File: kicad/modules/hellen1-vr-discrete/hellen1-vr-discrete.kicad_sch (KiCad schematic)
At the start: 45 parts, among them M1 Module-vr-discrete-0.1, U1 74AHC1G02, U2 74AHC1G02, U751 SRV05-4, U753 MCP6004, U754 MAX9142, U755 NC7SB3157P6X, U756 NC7SB3157P6X

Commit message: vr-discrete: rename SRV05-4-P-T7 in kicad
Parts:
- U751: value SRV05-4 -> SRV05-4-P-T7
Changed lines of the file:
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@@
     (in_bom yes) (on_board yes)
     (property "Reference" "U751" (id 0) (at 76.2 30.48 0))
-    (property "Value" "SRV05-4" (id 1) (at 72.39 26.67 0)
+    (property "Value" "SRV05-4-P-T7" (id 1) (at 72.39 26.67 0)
       (effects (font (size 1.27 1.27)) hide)
     )
@@
     )
     (path "/2438cbe3-a2c4-4bca-9f38-14e827595b8e"
-      (reference "U751") (unit 1) (value "SRV05-4") (footprint "Package_TO_SOT_SMD:SOT-23-6")
+      (reference "U751") (unit 1) (value "SRV05-4-P-T7") (footprint "Package_TO_SOT_SMD:SOT-23-6")
     )
     (path "/4fab11ed-4e08-402e-943d-dbc4e18c69da"

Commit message: fix BOM/LED-GREEN-0603 for vr-discrete
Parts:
- D751: value LED -> LED-GREEN-0603
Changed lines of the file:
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@@
       (effects (font (size 1.27 1.27)) (justify right))
     )
-    (property "Value" "LED" (id 1) (at 33.4772 128.3208 90)
+    (property "Value" "LED-GREEN-0603" (id 1) (at 33.4772 128.3208 90)
       (effects (font (size 1.27 1.27)) (justify right))
     )
@@
     )
     (path "/f48b53a5-a1a7-45f8-861f-0a454ab7dbf2"
-      (reference "D751") (unit 1) (value "LED") (footprint "LED_SMD:LED_0603_1608Metric")
+      (reference "D751") (unit 1) (value "LED-GREEN-0603") (footprint "LED_SMD:LED_0603_1608Metric")
     )
     (path "/c56f9b22-fce5-4a58-bfa9-904429ba6336"

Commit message: vr-discrete: fix designator numbering
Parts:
- renumbered C1 to C761, M1 to M750, U1 to U752, U2 to U757
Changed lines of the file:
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@@
   (symbol (lib_id "Device:C") (at 219.71 77.47 0) (unit 1)
     (in_bom yes) (on_board yes)
-    (property "Reference" "C1" (id 0) (at 222.631 76.3016 0)
+    (property "Reference" "C761" (id 0) (at 222.631 76.3016 0)
       (effects (font (size 1.27 1.27)) (justify left))
     )
@@
   (symbol (lib_id "74xGxx:74AHC1G02") (at 203.2 64.77 0) (unit 1)
     (in_bom yes) (on_board yes)
-    (property "Reference" "U1" (id 0) (at 207.645 61.0828 0))
+    (property "Reference" "U752" (id 0) (at 207.645 61.0828 0))
     (property "Value" "74AHC1G02" (id 1) (at 211.455 63.3815 0))
     (property "Footprint" "Package_TO_SOT_SMD:SOT-23-5" (id 2) (at 203.2 64.77 0)
@@
   (symbol (lib_id "74xGxx:74AHC1G02") (at 203.2 78.74 0) (unit 1)
     (in_bom yes) (on_board yes)
-    (property "Reference" "U2" (id 0) (at 206.375 75.0528 0))
+    (property "Reference" "U757" (id 0) (at 206.375 75.0528 0))
     (property "Value" "74AHC1G02" (id 1) (at 211.455 77.3515 0))
     (property "Footprint" "Package_TO_SOT_SMD:SOT-23-5" (id 2) (at 203.2 78.74 0)
@@
   (symbol (lib_id "hellen-one-vr-discrete-0.1:Module-vr-discrete-0.1") (at 60.96 106.68 0) (unit 1)
     (in_bom yes) (on_board yes) (fields_autoplaced)
-    (property "Reference" "M1" (id 0) (at 77.47 103.3738 0))
+    (property "Reference" "M750" (id 0) (at 77.47 103.3738 0))
     (property "Value" "Module-vr-discrete-0.1" (id 1) (at 77.47 105.6725 0))
     (property "Footprint" "hellen-one-vr-discrete-0.1:vr-discrete" (id 2) (at 86.36 105.41 0)
@@
       (reference "#PWR0794") (unit 1) (value "GND") (footprint "")
     )
-    (path "/d48a1995-2c59-49e9-ae20-70b0acc08ff3"
-      (reference "C1") (unit 1) (value "1u") (footprint "Capacitor_SMD:C_0402_1005Metric")
-    )
     (path "/65804bb3-89db-493b-9774-afe58321711f"
       (reference "C751") (unit 1) (value "1n") (footprint "Capacitor_SMD:C_0402_1005Metric")
@@
       (reference "C760") (unit 1) (value "10n") (footprint "Capacitor_SMD:C_0402_1005Metric")
     )
+    (path "/d48a1995-2c59-49e9-ae20-70b0acc08ff3"
+      (reference "C761") (unit 1) (value "1u") (footprint "Capacitor_SMD:C_0402_1005Metric")
+    )
     (path "/68fa890e-ea5a-4f1e-b022-85af6082c1d3"
       (reference "C762") (unit 1) (value "1u") (footprint "Capacitor_SMD:C_0402_1005Metric")
@@
     )
     (path "/c56f9b22-fce5-4a58-bfa9-904429ba6336"
-      (reference "M1") (unit 1) (value "Module-vr-discrete-0.1") (footprint "hellen-one-vr-discrete-0.1:vr-discrete")
+      (reference "M750") (unit 1) (value "Module-vr-discrete-0.1") (footprint "hellen-one-vr-discrete-0.1:vr-discrete")
     )
     (path "/775a58d6-98a7-48ae-b469-7148a9e02d9b"
@@
       (reference "R769") (unit 1) (value "10") (footprint "Resistor_SMD:R_0402_1005Metric")
     )
-    (path "/74280eea-e894-4ce8-bacd-e9b7722ccb6d"
-      (reference "U1") (unit 1) (value "74AHC1G02") (footprint "Package_TO_SOT_SMD:SOT-23-5")
-    )
-    (path "/f71d842a-9b40-4ac0-a243-11a16b8f8a76"
-      (reference "U2") (unit 1) (value "74AHC1G02") (footprint "Package_TO_SOT_SMD:SOT-23-5")
-    )
     (path "/2438cbe3-a2c4-4bca-9f38-14e827595b8e"
       (reference "U751") (unit 1) (value "SRV05-4-P-T7") (footprint "Package_TO_SOT_SMD:SOT-23-6")
     )
+    (path "/74280eea-e894-4ce8-bacd-e9b7722ccb6d"
+      (reference "U752") (unit 1) (value "74AHC1G02") (footprint "Package_TO_SOT_SMD:SOT-23-5")
+    )
     (path "/4fab11ed-4e08-402e-943d-dbc4e18c69da"
       (reference "U753") (unit 1) (value "MCP6004") (footprint "Package_SO:TSSOP-14_4.4x5mm_P0.65mm")
@@
       (reference "U756") (unit 2) (value "NC7SB3157P6X") (footprint "Package_TO_SOT_SMD:SOT-363_SC-70-6")
     )
-  )
+    (path "/f71d842a-9b40-4ac0-a243-11a16b8f8a76"
+      (reference "U757") (unit 1) (value "74AHC1G02") (footprint "Package_TO_SOT_SMD:SOT-23-5")
+    )
+  )

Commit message: VR 0.2 progress
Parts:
- removed M750: Module-vr-discrete-0.1, hellen-one-vr-discrete-0.1:vr-discrete, symbol hellen-one-vr-discrete-0.1:Module-vr-discrete-0.1
- added M750: Module-vr-discrete-0.2, hellen-one-vr-discrete-0.2:vr-discrete, symbol vr-discrete:Module-vr-discrete-0.2
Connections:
- net +5V: now also M750.E4 (V5_IN)
- net GND: now also M750.G (GND)
- net VR+: now also M750.W2 (VR+)
- net VR-: now also M750.W1 (VR-)
- net analog_out: now also M750.E2 (OUT_A)
- net output: now also M750.E3 (OUT)
- net thresh_input: now also M750.E1 (Thresh_IN)

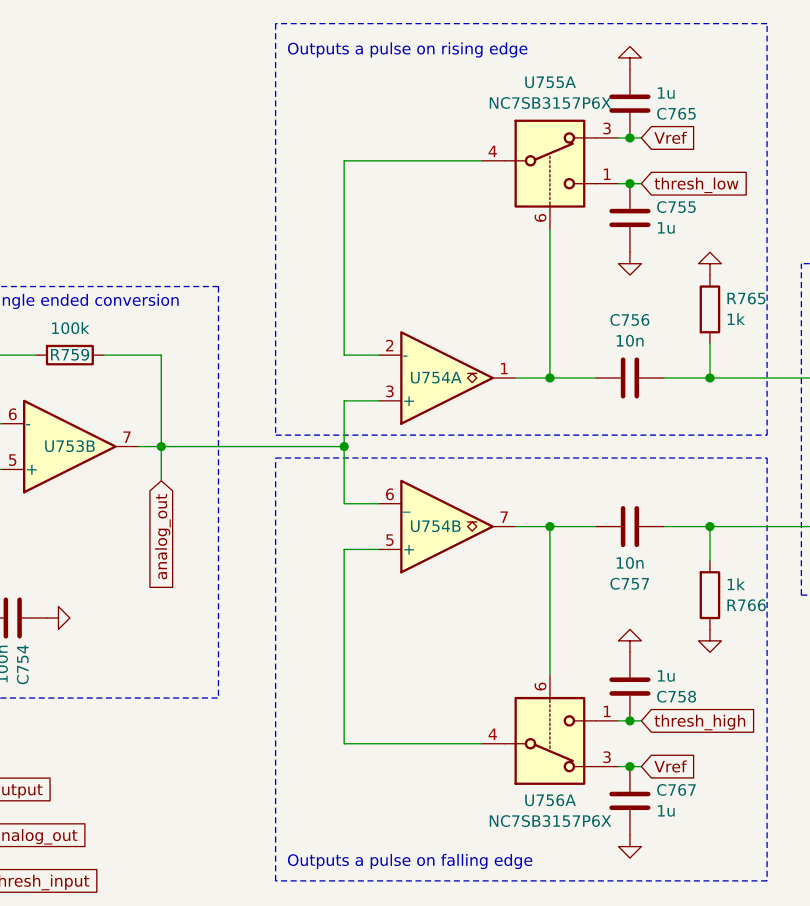
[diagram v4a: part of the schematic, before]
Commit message: ver 0.4
add C768, C769 (#247)
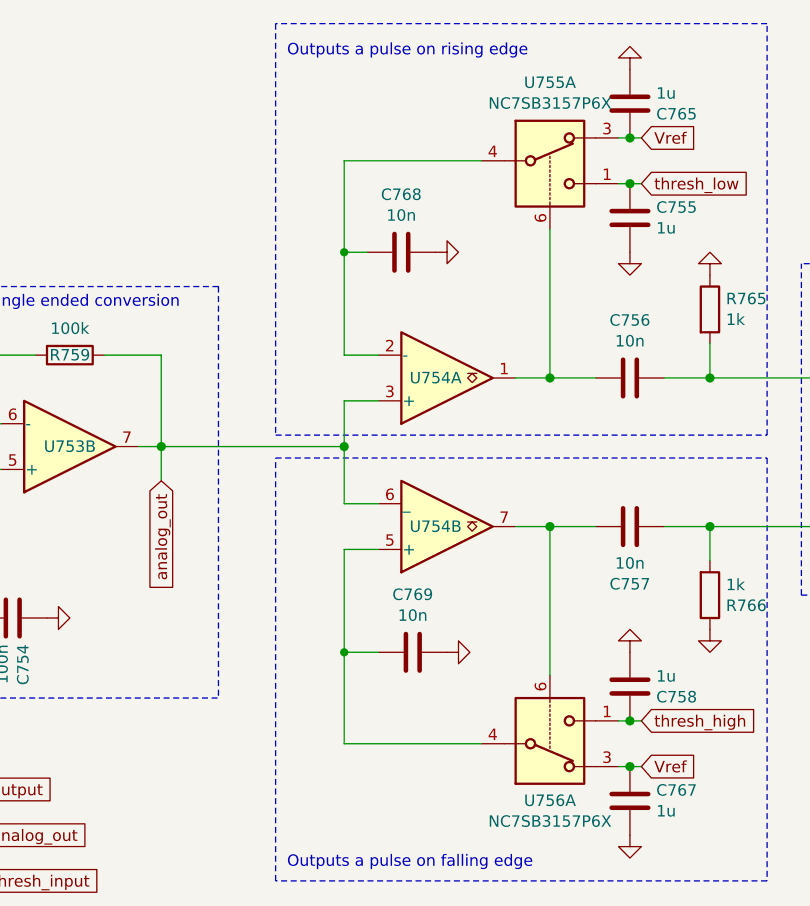
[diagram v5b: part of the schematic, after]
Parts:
- added C768, C769: 10n, Capacitor_SMD:C_0402_1005Metric, symbol Device:C
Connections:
- net GND: now also C768.1, C769.1
- net at U754.5 (+), U756.4: now also C769.2
- net at U754.2 (-), U755.4: now also C768.2
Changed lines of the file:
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@@
   (junction (at 142.24 71.12) (diameter 1.016) (color 0 0 0 0)
   )
+  (junction (at 142.24 93.98) (diameter 0) (color 0 0 0 0)
+  )
   (junction (at 264.16 105.41) (diameter 1.016) (color 0 0 0 0)
   )
@@
   )
   (junction (at 120.65 147.32) (diameter 1.016) (color 0 0 0 0)
+  )
+  (junction (at 142.24 49.53) (diameter 0) (color 0 0 0 0)
   )
   (junction (at 165.1 63.5) (diameter 1.016) (color 0 0 0 0)
@@
     (stroke (width 0) (type solid) (color 0 0 0 0))
   )
+  (wire (pts (xy 142.24 93.98) (xy 146.05 93.98))
+    (stroke (width 0) (type default) (color 0 0 0 0))
+  )
   (wire (pts (xy 157.48 138.43) (xy 153.67 138.43))
     (stroke (width 0) (type solid) (color 0 0 0 0))
@@
     (stroke (width 0) (type solid) (color 0 0 0 0))
   )
+  (wire (pts (xy 142.24 93.98) (xy 142.24 104.14))
+    (stroke (width 0) (type solid) (color 0 0 0 0))
+  )
   (wire (pts (xy 194.31 72.39) (xy 212.09 69.85))
     (stroke (width 0) (type solid) (color 0 0 0 0))
@@
   (wire (pts (xy 254 105.41) (xy 264.16 105.41))
     (stroke (width 0) (type solid) (color 0 0 0 0))
+  )
+  (wire (pts (xy 142.24 49.53) (xy 144.78 49.53))
+    (stroke (width 0) (type default) (color 0 0 0 0))
   )
   (wire (pts (xy 157.48 39.37) (xy 142.24 39.37))
@@
     (stroke (width 0) (type solid) (color 0 0 0 0))
   )
+  (wire (pts (xy 142.24 49.53) (xy 142.24 60.96))
+    (stroke (width 0) (type solid) (color 0 0 0 0))
+  )
   (wire (pts (xy 73.66 68.58) (xy 91.44 68.58))
     (stroke (width 0) (type solid) (color 0 0 0 0))
@@
     (stroke (width 0) (type solid) (color 0 0 0 0))
   )
-  (wire (pts (xy 142.24 39.37) (xy 142.24 60.96))
+  (wire (pts (xy 142.24 39.37) (xy 142.24 49.53))
     (stroke (width 0) (type solid) (color 0 0 0 0))
   )
@@
     (stroke (width 0) (type solid) (color 0 0 0 0))
   )
-  (wire (pts (xy 142.24 82.55) (xy 142.24 104.14))
+  (wire (pts (xy 142.24 82.55) (xy 142.24 93.98))
     (stroke (width 0) (type solid) (color 0 0 0 0))
   )
@@
       (effects (font (size 1.27 1.27)) hide)
     )
+  )
+  (symbol (lib_id "power:GND") (at 153.67 93.98 90) (mirror x) (unit 1)
+    (in_bom yes) (on_board yes)
+    (property "Reference" "#PWR072" (id 0) (at 160.02 93.98 0)
+      (effects (font (size 1.27 1.27)) hide)
+    )
+    (property "Value" "GND" (id 1) (at 158.0642 94.107 0)
+      (effects (font (size 1.27 1.27)) hide)
+    )
+    (property "Footprint" "" (id 2) (at 153.67 93.98 0)
+      (effects (font (size 1.27 1.27)) hide)
+    )
+    (property "Datasheet" "" (id 3) (at 153.67 93.98 0)
+      (effects (font (size 1.27 1.27)) hide)
+    )
+    (pin "1")
   )
   (symbol (lib_id "Device:C") (at 173.99 97.79 0) (mirror x) (unit 1)
@@
     (pin "1")
   )
+  (symbol (lib_id "Device:C") (at 149.86 93.98 270) (unit 1)
+    (in_bom yes) (on_board yes)
+    (property "Reference" "C769" (id 0) (at 149.86 87.5792 90))
+    (property "Value" "10n" (id 1) (at 149.86 89.8906 90))
+    (property "Footprint" "Capacitor_SMD:C_0402_1005Metric" (id 2) (at 146.05 94.9452 0)
+      (effects (font (size 1.27 1.27)) hide)
+    )
+    (property "Datasheet" "~" (id 3) (at 149.86 93.98 0)
+      (effects (font (size 1.27 1.27)) hide)
+    )
+    (property "LCSC" "C15195" (id 4) (at 149.86 93.98 0)
+      (effects (font (size 1.27 1.27)) hide)
+    )
+    (pin "1")
+    (pin "2")
+  )
   (symbol (lib_id "Device:C") (at 254 85.09 0) (unit 1)
     (in_bom yes) (on_board yes)
@@
     (pin "1")
   )
+  (symbol (lib_id "power:GND") (at 152.4 49.53 90) (mirror x) (unit 1)
+    (in_bom yes) (on_board yes)
+    (property "Reference" "#PWR071" (id 0) (at 158.75 49.53 0)
+      (effects (font (size 1.27 1.27)) hide)
+    )
+    (property "Value" "GND" (id 1) (at 156.7942 49.657 0)
+      (effects (font (size 1.27 1.27)) hide)
+    )
+    (property "Footprint" "" (id 2) (at 152.4 49.53 0)
+      (effects (font (size 1.27 1.27)) hide)
+    )
+    (property "Datasheet" "" (id 3) (at 152.4 49.53 0)
+      (effects (font (size 1.27 1.27)) hide)
+    )
+    (pin "1")
+  )
   (symbol (lib_id "Analog_Switch:NC7SB3157P6X") (at 165.1 36.83 0) (unit 1)
     (in_bom yes) (on_board yes)
@@
     (pin "2")
   )
+  (symbol (lib_id "Device:C") (at 148.59 49.53 270) (unit 1)
+    (in_bom yes) (on_board yes)
+    (property "Reference" "C768" (id 0) (at 148.59 43.1292 90))
+    (property "Value" "10n" (id 1) (at 148.59 45.4406 90))
+    (property "Footprint" "Capacitor_SMD:C_0402_1005Metric" (id 2) (at 144.78 50.4952 0)
+      (effects (font (size 1.27 1.27)) hide)
+    )
+    (property "Datasheet" "~" (id 3) (at 148.59 49.53 0)
+      (effects (font (size 1.27 1.27)) hide)
+    )
+    (property "LCSC" "C15195" (id 4) (at 148.59 49.53 0)
+      (effects (font (size 1.27 1.27)) hide)
+    )
+    (pin "1")
+    (pin "2")
+  )
   (symbol (lib_id "Analog_Switch:NC7SB3157P6X") (at 273.05 55.88 0) (unit 2)
     (in_bom yes) (on_board yes)
@@
       (reference "#PWR04") (unit 1) (value "GND") (footprint "")
     )
+    (path "/424efb71-c533-48ee-a69e-48157af84f19"
+      (reference "#PWR071") (unit 1) (value "GND") (footprint "")
+    )
+    (path "/01df23ab-f38b-4e99-9068-ed88cd9a2d2f"
+      (reference "#PWR072") (unit 1) (value "GND") (footprint "")
+    )
     (path "/c3adb51c-3c09-4ed2-bff5-ae9ac0e8fc71"
       (reference "#PWR0751") (unit 1) (value "+5V") (footprint "")
@@
       (reference "C767") (unit 1) (value "1u") (footprint "Capacitor_SMD:C_0402_1005Metric")
     )
+    (path "/e5a1cdae-199a-4046-80ee-ce9e705b9567"
+      (reference "C768") (unit 1) (value "10n") (footprint "Capacitor_SMD:C_0402_1005Metric")
+    )
+    (path "/1cb49e6f-7a31-4674-9884-6cb36e7228b5"
+      (reference "C769") (unit 1) (value "10n") (footprint "Capacitor_SMD:C_0402_1005Metric")
+    )
     (path "/f48b53a5-a1a7-45f8-861f-0a454ab7dbf2"

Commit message: vr-discrete 0.5 #375
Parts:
- removed M750: Module-vr-discrete-0.2, hellen-one-vr-discrete-0.2:vr-discrete, symbol vr-discrete:Module-vr-discrete-0.2
- added M750: Module-vr-discrete-0.5, hellen-one-vr-discrete-0.5:vr-discrete, symbol vr-discrete:Module-vr-discrete-0.5
- added R770: DNP, Resistor_SMD:R_0402_1005Metric, symbol Device:R
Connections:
- net +5V: now also M750.E4 (V5_IN)
- net GND: now also M750.G (GND)
- net VR+: now also M750.W2 (VR+)
- net VR-: now also M750.W1 (VR-)
- net analog_out: now also M750.E2 (OUT_A)
- net output: now also M750.E3 (OUT)
- net thresh_input: now also M750.E1 (Thresh_IN)
- net at C751.2, R753.1, R756.1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: now also R770.2
- net at C751.1, R752.2, R755.2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: now also R770.1
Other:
- note added: "Install R770 for use with very hot VR signals, to dampen the signal"
